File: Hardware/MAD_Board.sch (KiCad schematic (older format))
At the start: 73 parts, among them J1 Conn_02x05_Odd_Even, J10 Conn_01x05, J2 Conn_02x05_Odd_Even, J3 Conn_02x05_Odd_Even, J4 Conn_02x05_Odd_Even, J5 Conn_02x03_Odd_Even, J7 Power, J8 USB_B_Micro, J9 Micro_SD_Card, P10 CONN_01X01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

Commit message: small fixes
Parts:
- C15: LSCS Part # C19702 -> C15850
- C17, C5, C6: LSCS Part # C14663 -> C15850
- D2, D4, D5: LCSC C2286 -> C84256; LCSC Part # C2286 -> C84256; LSCS Part # C2286 -> C84256
- D6: value BLUE -> RED; LCSC C72041 -> C84256; LCSC Part # C72041 -> C84256; LSCS Part # C72041 -> C84256
- R14, R15, R17: LCSC C23350 -> C25221; LCSC Part # C23350 -> C25221; LSCS Part # C23350 -> C25221
- R5: value 240R -> 620R; LCSC C23350 -> C23220; LCSC Part # C23350 -> C23220; LSCS Part # C23350 -> C23220
- R6: value 100R -> 240R; LCSC C22775 -> C25221; LCSC Part # C22775 -> C25221; LSCS Part # C22775 -> C25221
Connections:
- net P0: no longer P6.8 (Pin_8)
- net P1: no longer P6.7 (Pin_7)
- net P11: no longer P5.7 (Pin_7)
- net P12: no longer P5.6 (Pin_6)
- net P13: no longer P5.5 (Pin_5)
- net P14: no longer P5.2 (Pin_2)
- net P15: no longer P5.1 (Pin_1)
- net P2: no longer P6.6 (Pin_6)
- net P3: no longer P6.5 (Pin_5)
- net P4: no longer P6.4 (Pin_4)
- net P5: no longer P6.3 (Pin_3)
- net P6: no longer P6.2 (Pin_2)
- no-connect marks 36 -> 48
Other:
- note added: "TESTING NOTES:\n- EEPROM soldered in wrong way\n- Fixed status leds resistor values to 5mA"

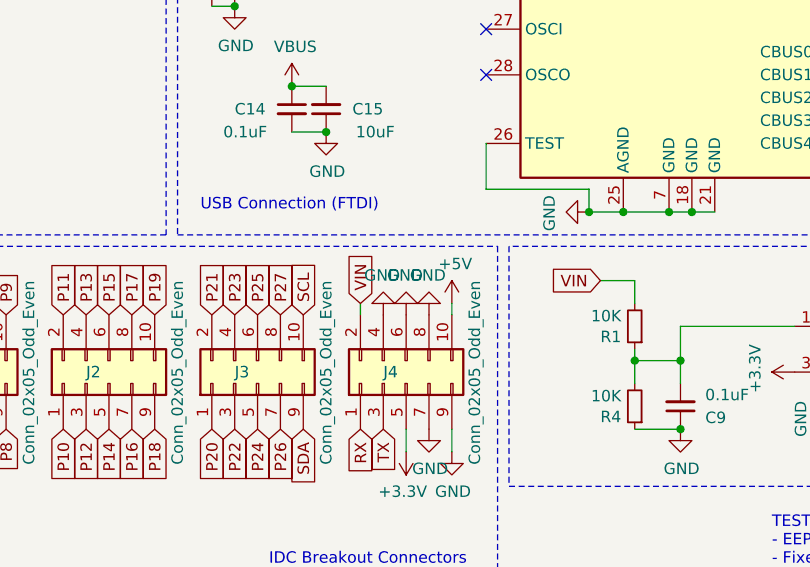
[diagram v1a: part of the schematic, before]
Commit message: updated schematic renders
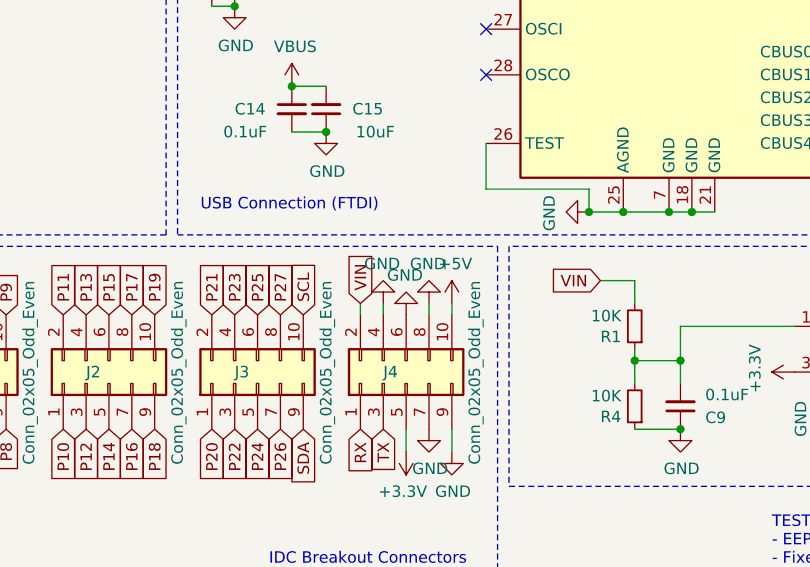
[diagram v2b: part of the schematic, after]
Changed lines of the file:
@@
 L power:GND #PWR014
 U 1 1 602D02ED
-P 5550 5750
-F 0 "#PWR014" H 5550 5500 50  0001 C CNN
-F 1 "GND" H 5555 5577 50  0000 C CNN
-F 2 "" H 5550 5750 50  0001 C CNN
-F 3 "" H 5550 5750 50  0001 C CNN
-	1    5550 5750
+P 5550 5700
+F 0 "#PWR014" H 5550 5450 50  0001 C CNN
+F 1 "GND" H 5555 5527 50  0000 C CNN
+F 2 "" H 5550 5700 50  0001 C CNN
+F 3 "" H 5550 5700 50  0001 C CNN
+	1    5550 5700
 	-1   0    0    1
 $EndComp
@@
 L power:GND #PWR06
 U 1 1 602D092D
-P 5350 5750
-F 0 "#PWR06" H 5350 5500 50  0001 C CNN
-F 1 "GND" H 5355 5577 50  0000 C CNN
-F 2 "" H 5350 5750 50  0001 C CNN
-F 3 "" H 5350 5750 50  0001 C CNN
-	1    5350 5750
+P 5350 5700
+F 0 "#PWR06" H 5350 5450 50  0001 C CNN
+F 1 "GND" H 5355 5527 50  0000 C CNN
+F 2 "" H 5350 5700 50  0001 C CNN
+F 3 "" H 5350 5700 50  0001 C CNN
+	1    5350 5700
 	-1   0    0    1
 $EndComp
@@
 	1    0    0    -1
 $EndComp
+Wire Wire Line
+	5350 5750 5350 5700
+Wire Wire Line
+	5550 5750 5550 5700
 $EndSCHEMATC
